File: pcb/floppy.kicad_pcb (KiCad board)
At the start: 2 copper layers, 45.7 x 26.4 mm, 13 parts, among them J1 Conn_02x17_Odd_Even, J2 Conn_01x05, J3 USB_B, J4 Conn_01x04, U1 STM32L433CBTx, U2 L78L33_SOT89

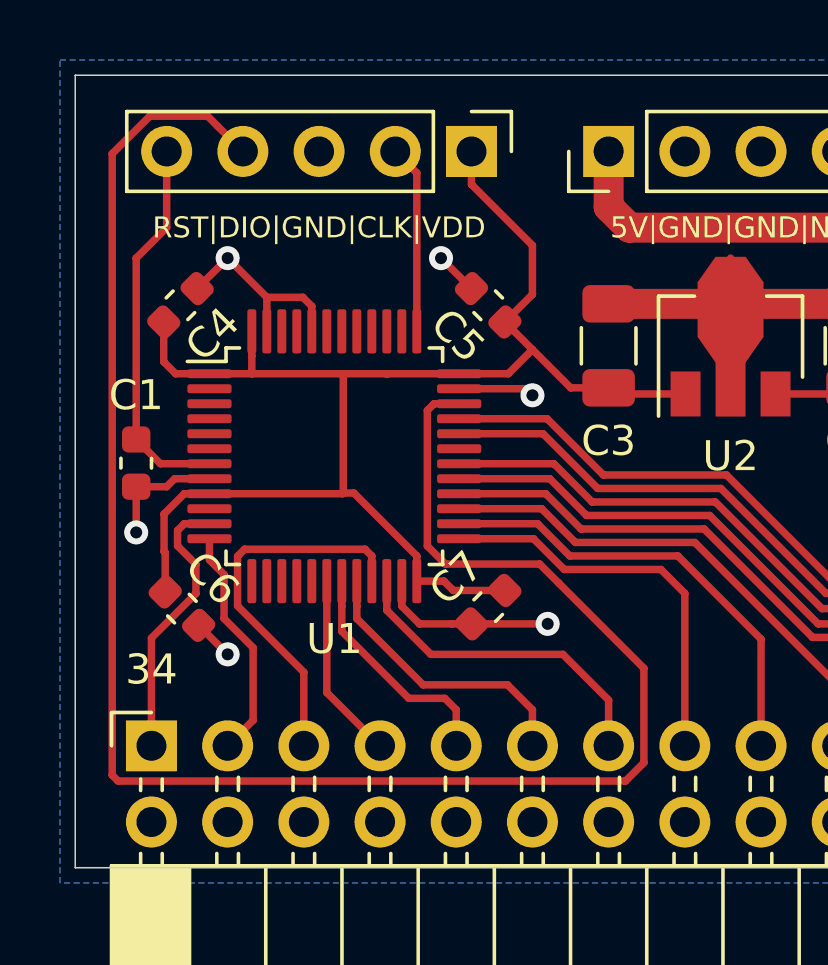
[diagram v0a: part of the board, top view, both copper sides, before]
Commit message: add USB software update jumper
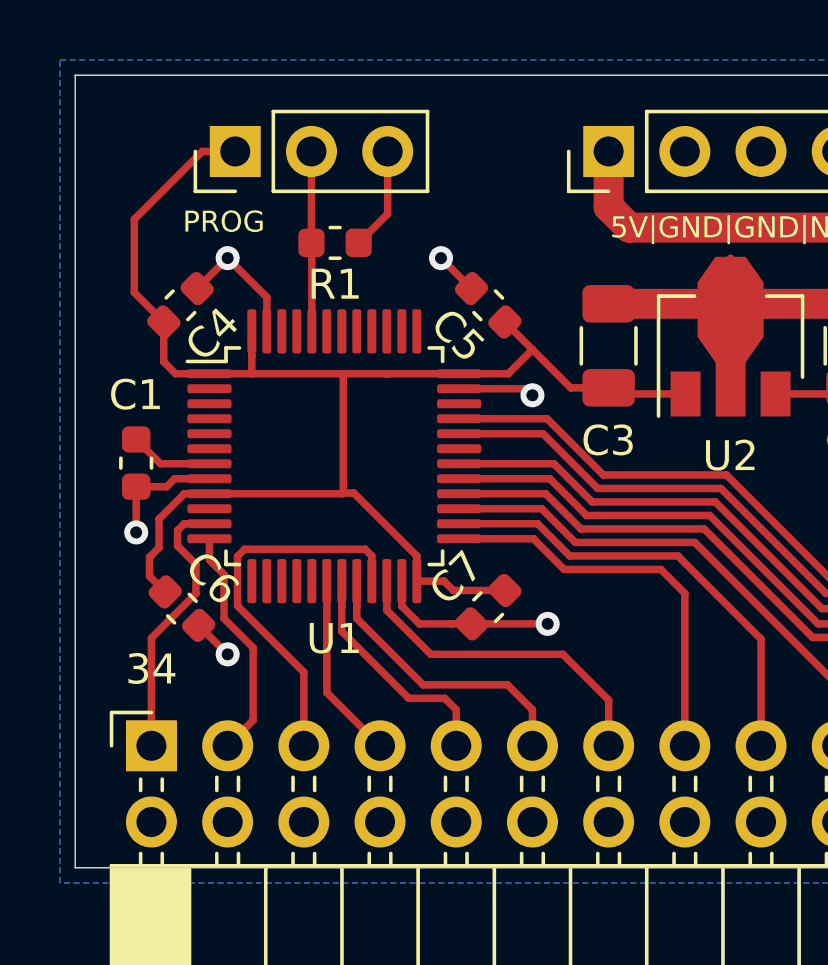
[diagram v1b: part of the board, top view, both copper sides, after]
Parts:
- added R1: 10k, Resistor_SMD:R_0603_1608Metric, F.Cu at (46.8, 47.2)
- J2: value Conn_01x05 -> PROG; footprint Connector_PinHeader_2.54mm:PinHeader_1x05_P2.54mm_Vertical -> Connector_PinHeader_2.54mm:PinHeader_1x03_P2.54mm_Vertical
- moved J2 7.87 mm to (43.4, 44.2), turned to 90 degrees
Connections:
- J2 pad 2: SWCLK -> BOOT0
- U1 pad 34: SWDIO -> Net-(U1-Pad34)
- U1 pad 37: SWCLK -> Net-(U1-Pad37)
- U1 pad 44: GND -> BOOT0
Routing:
- net SWDIO: track 61.9 -> 0.00 mm
- net NRST: track 12.8 -> 2.78 mm
- net SWCLK: track 6.29 -> 0.00 mm
- net BOOT0: track 0.00 -> 6.00 mm
- net +3V3: track 49.6 -> 51.2 mm
- net GND: track 40.5 -> 41.5 mm
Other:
- board text added: "PROG"
- board text added: "USB Floppy v1.1"
- board text removed: "RST|DIO|GND|CLK|VDD"
- board text removed: "USB Floppy v1.0"

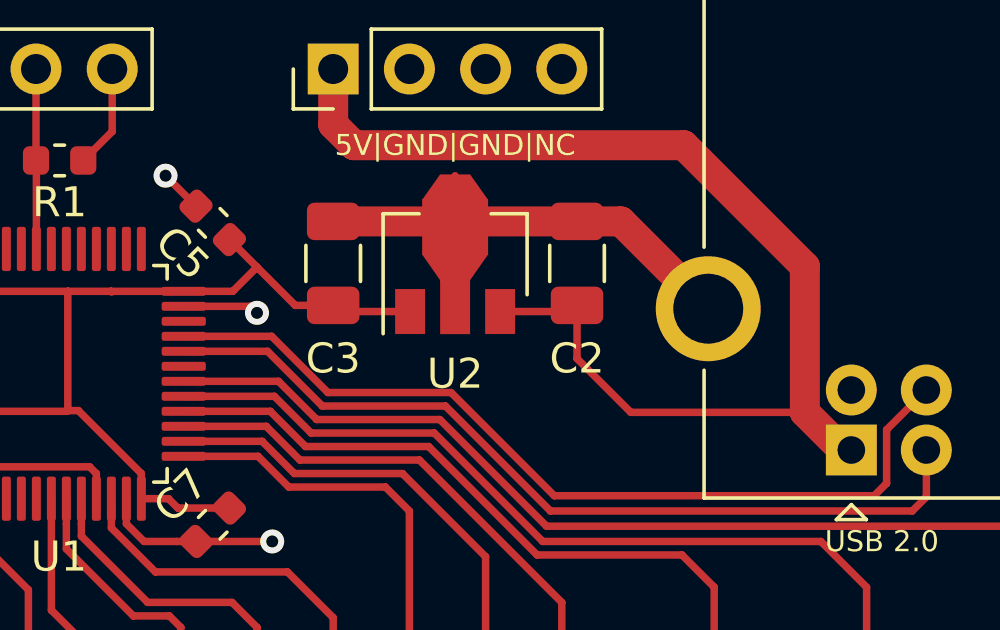
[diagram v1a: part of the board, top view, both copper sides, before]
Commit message: reduce large capacitors
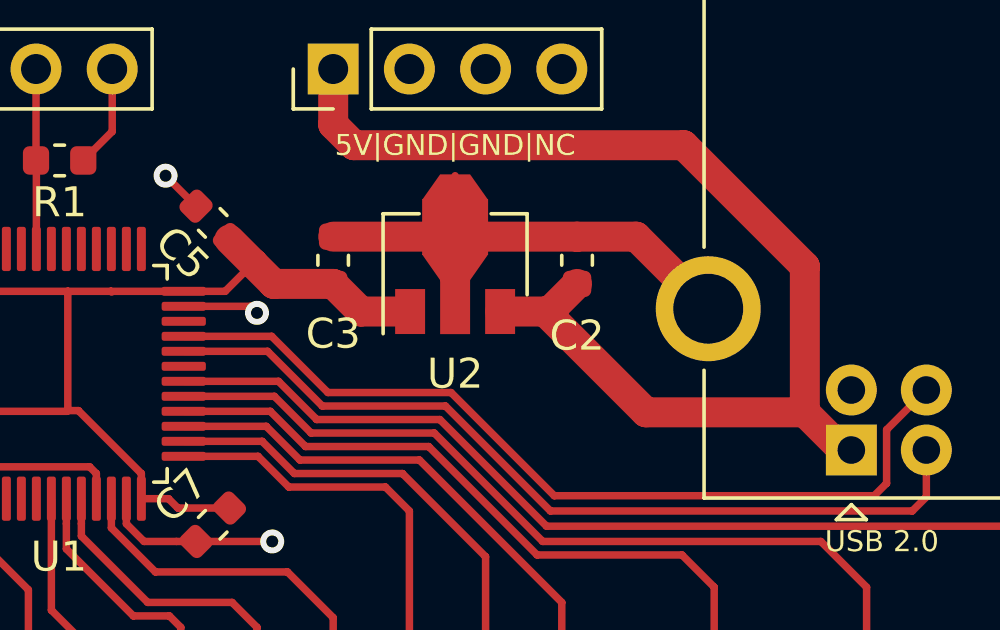
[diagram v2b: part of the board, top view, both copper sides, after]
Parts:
- C2, C3: value 10u -> 4.7u; footprint Capacitor_SMD:C_1206_3216Metric -> Capacitor_SMD:C_0603_1608Metric
- moved C2 0.10 mm to (64.0, 50.6)
- moved C3 0.10 mm to (55.9, 50.6)
